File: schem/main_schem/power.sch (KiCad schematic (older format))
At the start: 5 parts, among them U6 LM7805, U7 LM1117-3.3

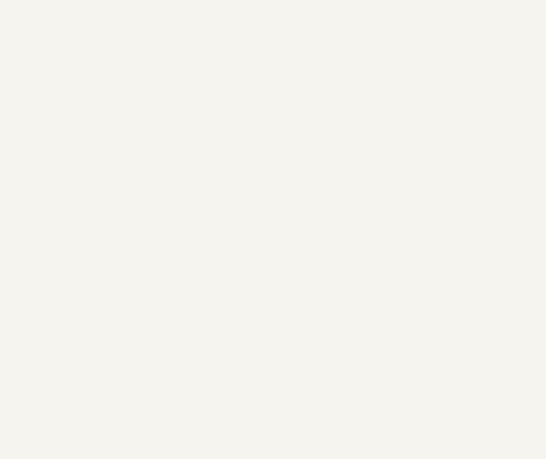
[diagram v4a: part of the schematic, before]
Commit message: Power connector, update led footprint, update TODO, route power traces
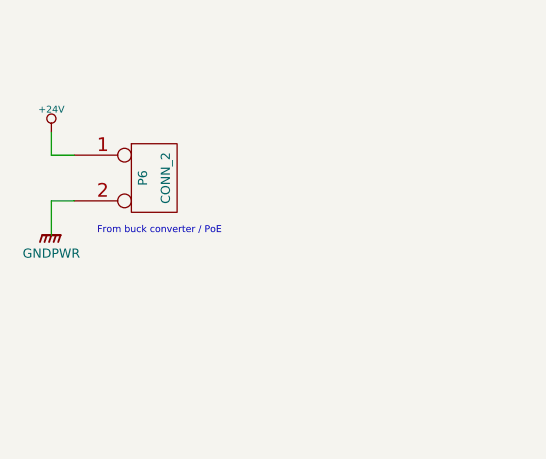
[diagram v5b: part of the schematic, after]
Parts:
- added P6: CONN_2, symbol CONN_2
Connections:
- net +24V: now also P6.1 (P1)
- net GND: now also P6.2 (PM)
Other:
- note added: "From buck converter / PoE"
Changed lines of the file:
@@
-EESchema Schematic File Version 2  date 10/20/2012 6:17:28 PM
+EESchema Schematic File Version 2  date 10/22/2012 10:04:33 AM
 LIBS:power
 LIBS:device
@@
 Sheet 5 6
 Title "Power Subsystem"
-Date "20 oct 2012"
+Date "22 oct 2012"
 Rev ""
 Comp "Ingersoll Rand 402 Senior Design group."
@@
 Comment4 ""
 $EndDescr
-Text Notes 9700 800  0    30   ~ 0
-These grounds should be connected via single points only,\n possibly with ferrite beads between them to minimize transients.
+Text Notes 1700 1450 0    30   ~ 0
+From buck converter / PoE
+Wire Wire Line
+	1500 1450 1500 1300
+Wire Wire Line
+	1500 1300 1600 1300
 Connection ~ 10250 900
 Wire Wire Line
@@
 Wire Wire Line
 	10250 900  10250 1000
-$Comp
-L GNDPWR #PWR68
+Wire Wire Line
+	1500 1000 1500 1100
+Wire Wire Line
+	1500 1100 1600 1100
+$Comp
+L GNDPWR #PWR058
+U 1 1 50847215
+P 1500 1450
+F 0 "#PWR058" H 1500 1500 40  0001 C CNN
+F 1 "GNDPWR" H 1500 1370 40  0000 C CNN
+	1    1500 1450
+	1    0    0    -1
+$EndComp
+$Comp
+L +24V #PWR059
+U 1 1 50847204
+P 1500 1000
+F 0 "#PWR059" H 1500 950 20  0001 C CNN
+F 1 "+24V" H 1500 1100 30  0000 C CNN
+	1    1500 1000
+	1    0    0    -1
+$EndComp
+$Comp
+L CONN_2 P6
+U 1 1 508471EA
+P 1950 1200
+F 0 "P6" V 1900 1200 40  0000 C CNN
+F 1 "CONN_2" V 2000 1200 40  0000 C CNN
+	1    1950 1200
+	1    0    0    -1
+$EndComp
+Text Notes 9700 800  0    30   ~ 0
+These grounds should be connected via single points only,\n possibly with ferrite beads between them to minimize transients.
+$Comp
+L GNDPWR #PWR060
 U 1 1 50674BFE
 P 10650 1000
-F 0 "#PWR68" H 10650 1050 40  0001 C CNN
+F 0 "#PWR060" H 10650 1050 40  0001 C CNN
 F 1 "GNDPWR" H 10650 920 40  0000 C CNN
 	1    10650 1000
@@
 $EndComp
 $Comp
-L VSS #PWR67
+L VSS #PWR061
 U 1 1 50674BEC
 P 10250 1000
-F 0 "#PWR67" H 10250 1000 30  0001 C CNN
+F 0 "#PWR061" H 10250 1000 30  0001 C CNN
 F 1 "VSS" H 10250 930 30  0000 C CNN
 	1    10250 1000
@@
 $EndComp
 $Comp
-L GND #PWR66
+L GND #PWR062
 U 1 1 50674BE7
 P 9850 1000
-F 0 "#PWR66" H 9850 1000 30  0001 C CNN
+F 0 "#PWR062" H 9850 1000 30  0001 C CNN
 F 1 "GND" H 9850 930 30  0001 C CNN
 	1    9850 1000
@@
 DIGITAL SYSTEM REGULATORS
 $Comp
-L GND #PWR65
+L GND #PWR063
 U 1 1 50674B55
 P 9450 2050
-F 0 "#PWR65" H 9450 2050 30  0001 C CNN
+F 0 "#PWR063" H 9450 2050 30  0001 C CNN
 F 1 "GND" H 9450 1980 30  0001 C CNN
 	1    9450 2050
@@
 $EndComp
 $Comp
-L GND #PWR61
+L GND #PWR064
 U 1 1 50674B26
 P 8050 2050
-F 0 "#PWR61" H 8050 2050 30  0001 C CNN
+F 0 "#PWR064" H 8050 2050 30  0001 C CNN
 F 1 "GND" H 8050 1980 30  0001 C CNN
 	1    8050 2050
@@
 $EndComp
 $Comp
-L GND #PWR63
+L GND #PWR065
 U 1 1 50674B1A
 P 8800 2050
-F 0 "#PWR63" H 8800 2050 30  0001 C CNN
+F 0 "#PWR065" H 8800 2050 30  0001 C CNN
 F 1 "GND" H 8800 1980 30  0001 C CNN
 	1    8800 2050
@@
 $EndComp
 $Comp
-L +3.3V #PWR64
+L +3.3V #PWR066
 U 1 1 50674AF6
 P 9350 1100
-F 0 "#PWR64" H 9350 1060 30  0001 C CNN
+F 0 "#PWR066" H 9350 1060 30  0001 C CNN
 F 1 "+3.3V" H 9350 1210 30  0000 C CNN
 	1    9350 1100
@@
 $EndComp
 $Comp
-L GNDPWR #PWR59
+L GNDPWR #PWR067
 U 1 1 506749D8
 P 6900 2050
-F 0 "#PWR59" H 6900 2100 40  0001 C CNN
+F 0 "#PWR067" H 6900 2100 40  0001 C CNN
 F 1 "GNDPWR" H 6900 1970 40  0000 C CNN
 	1    6900 2050
@@
 $EndComp
 $Comp
-L GNDPWR #PWR60
+L GNDPWR #PWR068
 U 1 1 506749A3
 P 7450 2050
-F 0 "#PWR60" H 7450 2100 40  0001 C CNN
+F 0 "#PWR068" H 7450 2100 40  0001 C CNN
 F 1 "GNDPWR" H 7450 1970 40  0000 C CNN
 	1    7450 2050
@@
 $EndComp
 $Comp
-L +5V #PWR62
+L +5V #PWR069
 U 1 1 50674976
 P 8150 1100
-F 0 "#PWR62" H 8150 1190 20  0001 C CNN
+F 0 "#PWR069" H 8150 1190 20  0001 C CNN
 F 1 "+5V" H 8150 1190 30  0000 C CNN
 	1    8150 1100
@@
 $EndComp
 $Comp
-L +24V #PWR58
+L +24V #PWR070
 U 1 1 50674960
 P 6700 1100
-F 0 "#PWR58" H 6700 1050 20  0001 C CNN
+F 0 "#PWR070" H 6700 1050 20  0001 C CNN
 F 1 "+24V" H 6700 1200 30  0000 C CNN
 	1    6700 1100
